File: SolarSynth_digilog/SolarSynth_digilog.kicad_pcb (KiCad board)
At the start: 2 copper layers, 59.9 x 90 mm, 31 parts, among them J1 OutputJack1, J2 Conn_01x01_Pin, J3 Conn_01x01_Pin, P1 PiezoDisc, P2 PiezoDisc, U1 74HC14, U2 MCP6002-xMC

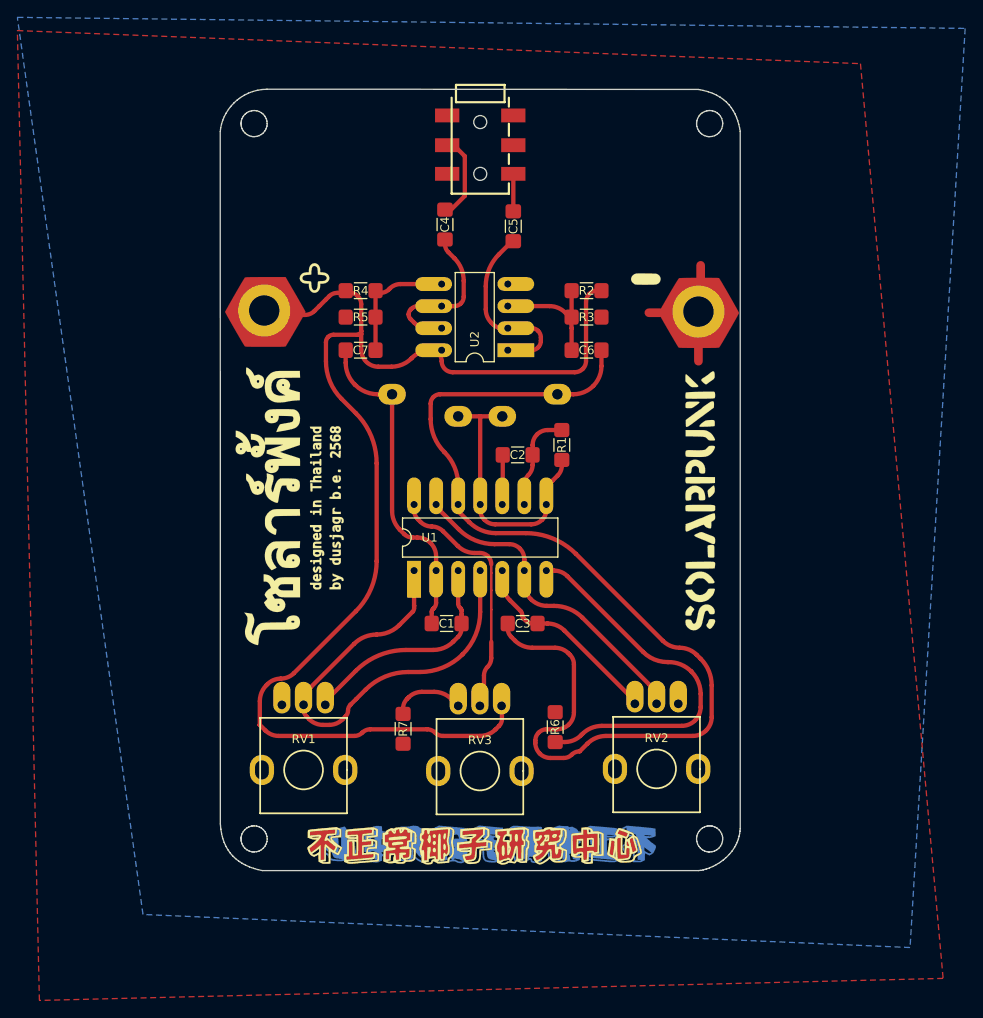
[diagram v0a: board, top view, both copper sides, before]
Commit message: Change SMD to THT
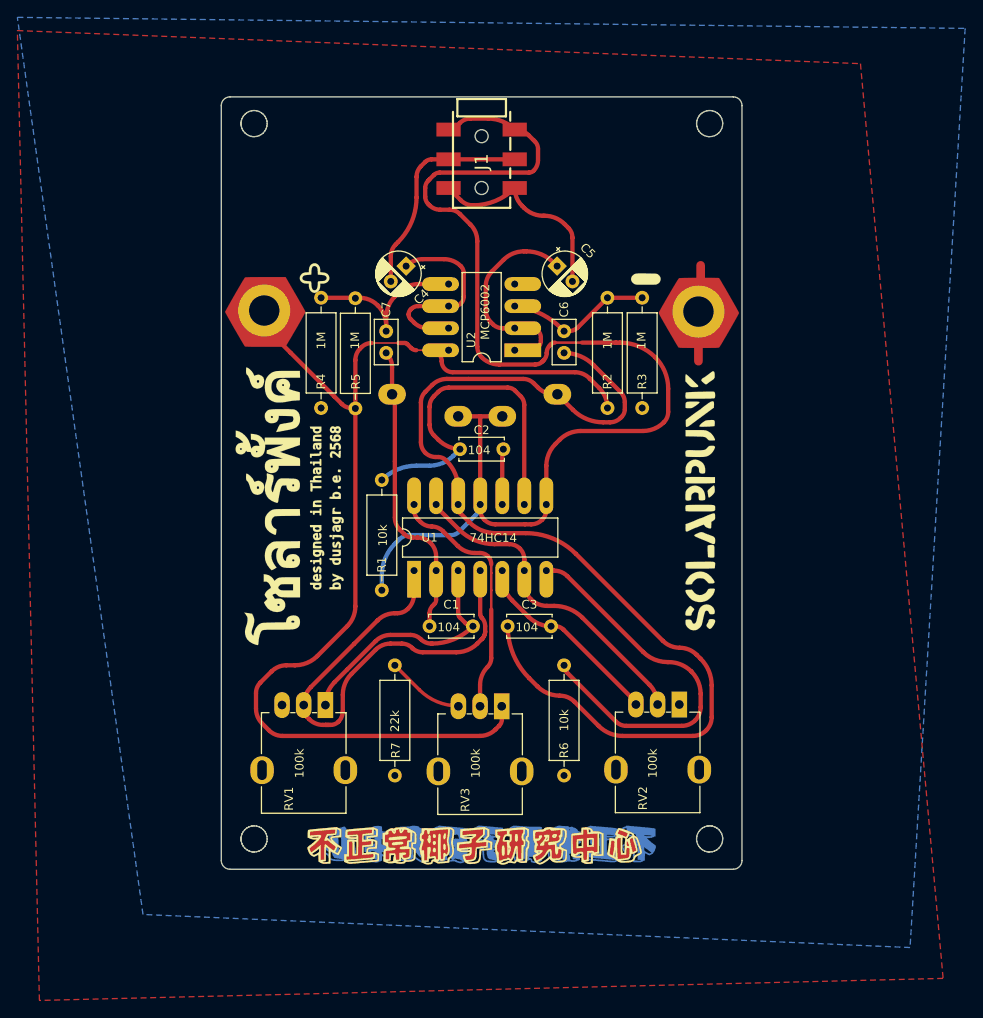
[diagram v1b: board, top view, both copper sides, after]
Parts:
- removed edge1: 5VBoard, 007_dusjagr:board_digilog
- C1, C2, C3: footprint 007_dusjagr:C_1210_noGND -> Capacitor_THT:C_Disc_D5.0mm_W2.5mm_P5.00mm
- C4, C5: footprint 007_dusjagr:C_1210_noGND -> Capacitor_THT:CP_Radial_D5.0mm_P2.50mm
- C6, C7: footprint 007_dusjagr:C_1210_noGND -> Capacitor_THT:C_Disc_D5.0mm_W2.5mm_P2.50mm
- R1, R2, R3, R4, R5, R6, R7: footprint 007_dusjagr:R_1206_noGND -> Resistor_THT:R_Axial_DIN0309_L9.0mm_D3.2mm_P12.70mm_Horizontal
- RV1, RV2, RV3: footprint 007_dusjagr:RD901F-ALPHA-3D_longpads -> blinkyparts:Potentiometer_Alpha_RD901F-40-00D_Single_Vertical_bigger-holes
- moved R1 26.7 mm to (105.5, 87.3)
- moved R2 13.7 mm to (131.5, 66.3), turned to 90 degrees
- moved R4 13.6 mm to (102.4, 66.4), turned to 90 degrees
- moved RV1 7.89 mm to (99.0, 100.6), turned to -90 degrees
- moved RV3 7.87 mm to (119.3, 100.7), turned to -90 degrees
- moved RV2 7.87 mm to (139.8, 100.5), turned to -90 degrees
- moved R7 7.38 mm to (107.0, 96.0)
- moved R6 7.20 mm to (126.5, 96.0), turned to -90 degrees
- moved C5 6.83 mm to (125.7, 50.0), turned to -45 degrees
- moved R3 6.79 mm to (135.5, 53.6), turned to -90 degrees
- moved C4 6.55 mm to (108.3, 50.0), turned to -135 degrees
- moved R5 5.07 mm to (98.5, 53.6), turned to -90 degrees
- moved C7 2.96 mm to (106.0, 60.0), turned to 90 degrees
- moved C6 2.61 mm to (126.5, 60.0), turned to 90 degrees
- moved C1 1.99 mm to (111.0, 91.5)
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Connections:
- J1 pad 1: GND -> Net-(Pad2-Pin_1)
- J3 pad 1: (no net) -> GND
- RV1 pad 1: unconnected-(RV1-Pad1) -> Net-(C1-Pad2)
- RV1 pad 3: Net-(C1-Pad2) -> unconnected-(RV1-Pad3)
- RV2 pad 1: Net-(C3-Pad2) -> unconnected-(RV2-Pad1)
- RV2 pad 3: unconnected-(RV2-Pad3) -> Net-(C3-Pad2)
- RV3 pad 1: Net-(R7-Pad1) -> VCC
- RV3 pad 3: VCC -> Net-(R7-Pad1)
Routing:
- net Net-(Pad2-Pin_1): track 30.9 -> 144.8 mm
- net Net-(C2-Pad2): track 11.4 -> 41.7 mm
- net Net-(C5-Pad2): track 4.32 -> 23.9 mm
- net VCC: track 140.9 -> 122.7 mm
- net Net-(C4-Pad2): track 11.0 -> 26.0 mm
- net Left: track 14.4 -> 20.6 mm
- net Net-(U2A--): track 25.2 -> 29.5 mm
- net Net-(RV1-Pad2): track 55.0 -> 58.7 mm
- net Right: track 14.3 -> 17.8 mm
- net Net-(Pad1-Pin_1): track 38.9 -> 35.5 mm
- net Net-(U2B--): track 19.2 -> 22.3 mm
- net Net-(Pad3-Pin_1): track 123.8 -> 126.7 mm
- net Net-(C1-Pad2): track 26.2 -> 29.0 mm
- net Net-(U1G-GND): track 43.9 -> 45.4 mm
- net GND: track 5.35 -> 4.08 mm
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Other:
- board size 59.9 x 90 mm -> 60 x 89 mm
- board text added: "100k"
- board text added: "104"
- board text added: "10k"
- board text added: "1M"
- board text added: "22k"
- board text added: "74HC14"
- board text added: "MCP6002"

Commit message: fixed some bugs
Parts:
- J1: footprint 007_dusjagr:AUDIO-JACK-3.5mm_SMD_Hole -> 002_Solarpunk:AUDIO-JACK-3.5mm_SMD_noHole
- J2, J3: footprint 007_dusjagr:SolarPad_VCC -> 002_Solarpunk:SolarPad_VCC
- Pad1, Pad2, Pad3, Pad4: footprint 007_dusjagr:SolderPad_small -> 002_Solarpunk:SolderPad_small
- U1: footprint 007_dusjagr:DIP-14_W7.62mm_LongerPads -> 002_Solarpunk:DIP-14_W7.62mm_LongerPads
- U2: footprint 007_dusjagr:DIP-8_W7.62mm_LongerPads -> Package_DIP:DIP-8_W7.62mm_LongPads
- moved R1 24.1 mm to (129.0, 82.0), turned to -45 degrees
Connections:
- J1 pad 1: Net-(Pad2-Pin_1) -> GND
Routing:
- net Net-(Pad2-Pin_1): track 144.8 -> 32.0 mm
- net Net-(C2-Pad2): track 41.7 -> 64.8 mm
- net VCC: track 122.7 -> 125.0 mm
- net GND: track 4.08 -> 5.10 mm
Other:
- board text added: "105"
- board text removed: "104"
